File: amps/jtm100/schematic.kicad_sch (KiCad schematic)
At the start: 82 parts, among them T1 OT

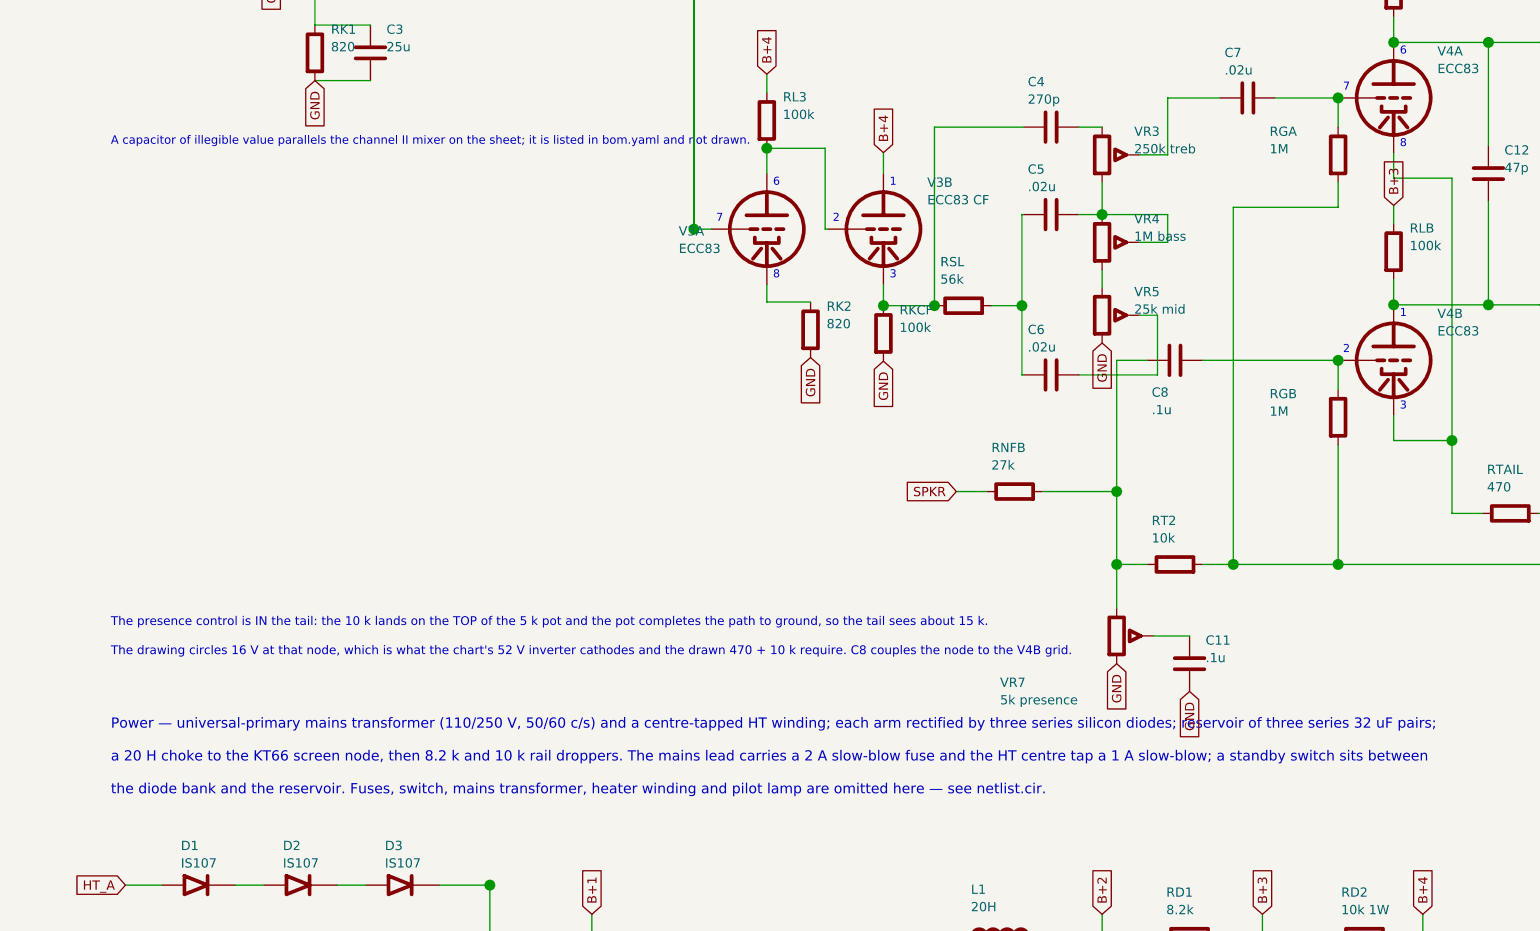
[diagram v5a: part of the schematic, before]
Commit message: Fix: schematic sheet notes no longer name repository files
Thirty-seven committed sheets rendered footnotes and section notes such as
"Heaters and PT primary omitted — see netlist.cir and meta.yaml" or
"excluded from netlist.cir (notes.md)" to visitors through KiCanvas. The
prose sweeps never counted sheets. Rewritten in the site's own words — the
netlist, the sources list, the circuit story, the parts list, the board
drawing — in 59 strings across 33 draw scripts, keeping every technical
claim as it was; the three tone sheets (6G4, 6G5, 6G6-B) are under repair
elsewhere and keep theirs for now. The sweep touched only strings passed to
the sheet's note, text, caption and footnote calls, never a path or a value.

Gates: check_schematics 40/0, connectivity 0 isolated pins;
verify_schematic_nets 40 clean; only the regenerated sheets and their served
copies changed.

Co-Authored-By: Claude Fable 5.1 <noreply@anthropic.com>
Claude-Session: https://claude.ai/code/session_01KBMfdh37HmCL2iWcBiL5J1
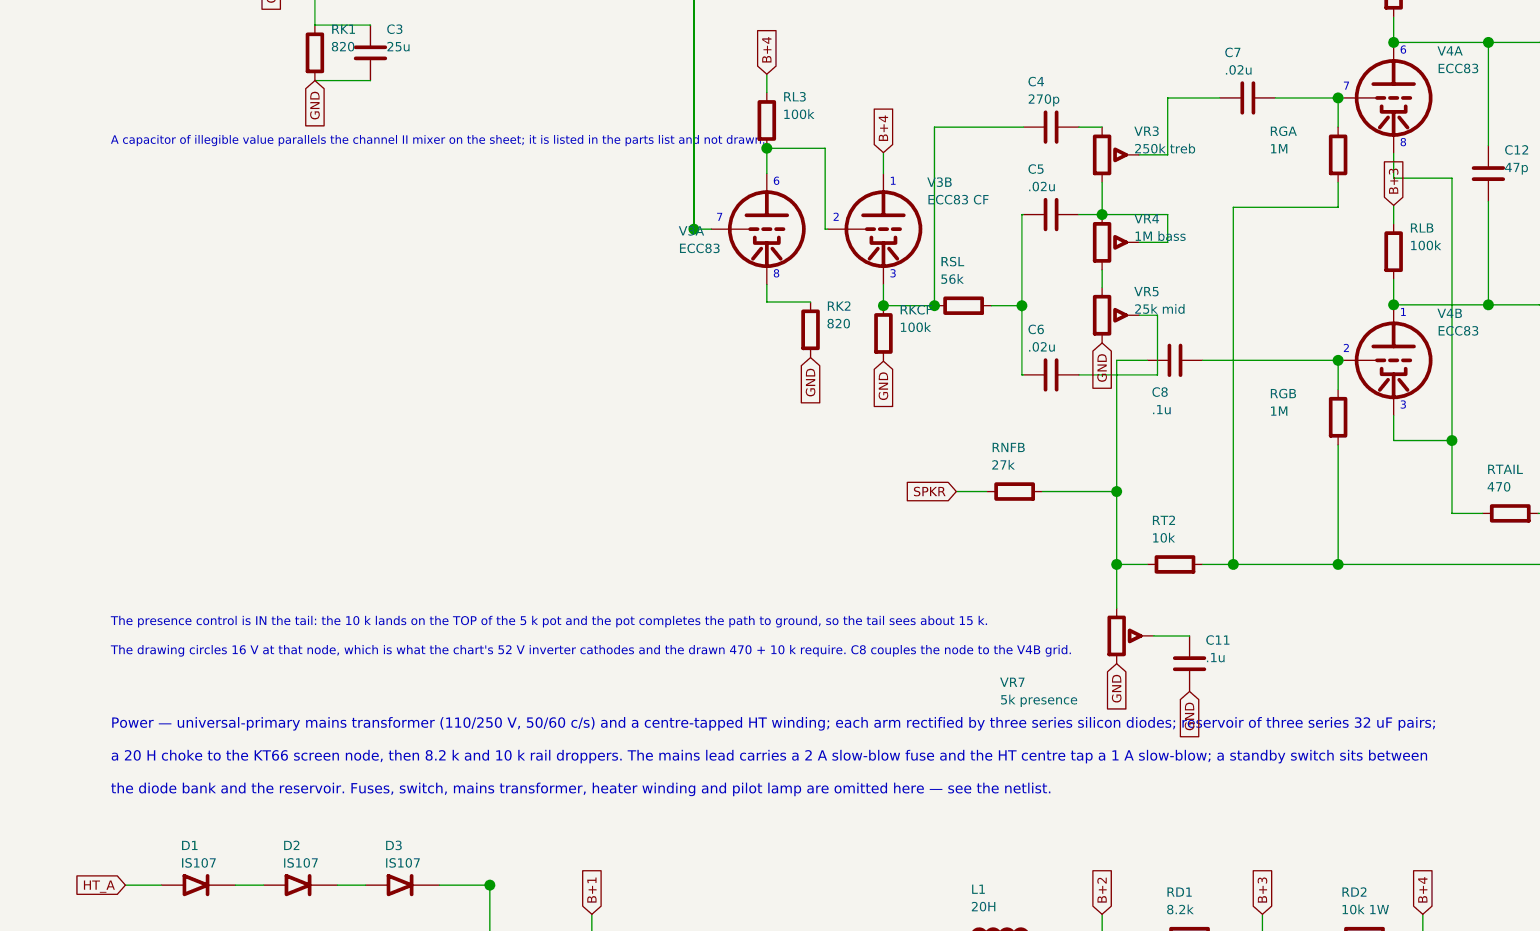
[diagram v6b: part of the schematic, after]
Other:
- note added: "A capacitor of illegible value parallels the channel II mixer on the sheet; it is listed in the parts list and not drawn."
- note added: "the diode bank and the reservoir. Fuses, switch, mains transformer, heater winding and pilot lamp are omitted here — see the netlist."
- note removed: "A capacitor of illegible value parallels the channel II mixer on the sheet; it is listed in bom.yaml and not drawn."
- note removed: "the diode bank and the reservoir. Fuses, switch, mains transformer, heater winding and pilot lamp are omitted here — see netlist.cir."
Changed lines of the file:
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@@
   (junction (at 101.336 66.988) (diameter 1.497) (color 0 0 0 0))
   (junction (at 101.336 118.278) (diameter 1.497) (color 0 0 0 0))
-  (text "A capacitor of illegible value parallels the channel II mixer on the sheet; it is listed in bom.yaml and not drawn." (at 21.336 106.278 0)
+  (text "A capacitor of illegible value parallels the channel II mixer on the sheet; it is listed in the parts list and not drawn." (at 21.336 106.278 0)
     (effects (font (size 1.15 1.15)) (justify left)))
   (wire (pts (xy 55.336 45.898) (xy 55.336 49.278))
@@
   (text "a 20 H choke to the KT66 screen node, then 8.2 k and 10 k rail droppers. The mains lead carries a 2 A slow-blow fuse and the HT centre tap a 1 A slow-blow; a standby switch sits between" (at 21.336 190.778 0)
     (effects (font (size 1.4 1.4)) (justify left)))
-  (text "the diode bank and the reservoir. Fuses, switch, mains transformer, heater winding and pilot lamp are omitted here — see netlist.cir." (at 21.336 195.278 0)
+  (text "the diode bank and the reservoir. Fuses, switch, mains transformer, heater winding and pilot lamp are omitted here — see the netlist." (at 21.336 195.278 0)
     (effects (font (size 1.4 1.4)) (justify left)))
   (global_label "HT_A" (shape input) (at 23.336 208.278 180)

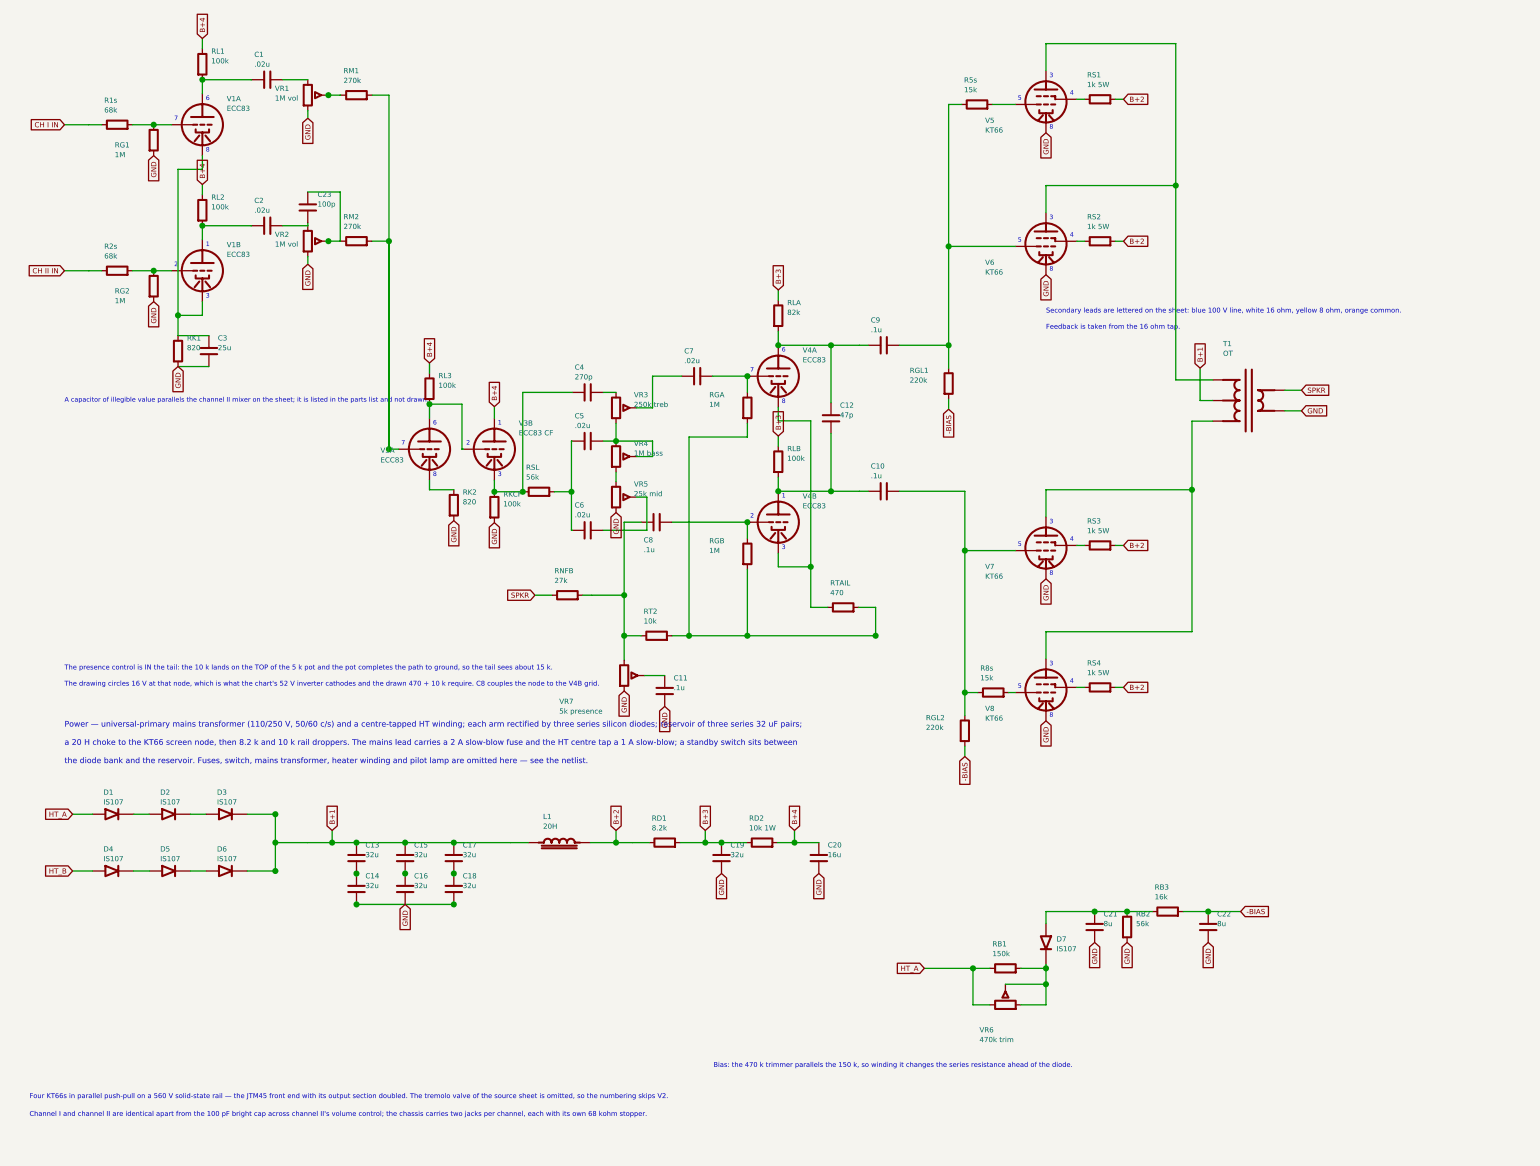
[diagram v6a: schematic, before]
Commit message: JTM100: each input jack has its own 68 kΩ stopper; leaks at jack 1's tip
The cited 1959T drawing (drtube 1959t-66.gif, 1068x759, sha1 94aa0ac9…)
draws four input jacks and four 68 Ks, two per channel (channel I pair crop
30,120,250,230 into V1A; channel II pair crop 30,230,250,340, its junction
running round to V1B's grid, crop 180,80,330,300), with each 1M from the
lower jack's tip line, jack side of its 68K, to ground. The BOM note said
the schematic draws one jack per channel, and the sheet hung the 1M on the
grid side of the stopper. R3s and R4s are added to the BOM and the sheet,
the leaks move to the jack-1 tip (R1s/R2s series_bridge in sch_map), and
the off-board scope glob widens to R[1-4]s. No DC node moves.

Co-Authored-By: Claude Opus 5.5 <noreply@anthropic.com>
Claude-Session: https://claude.ai/code/session_01KBMfdh37HmCL2iWcBiL5J1
Signed-off-by: AnalogMaker <theanalogmaker@gmail.com>
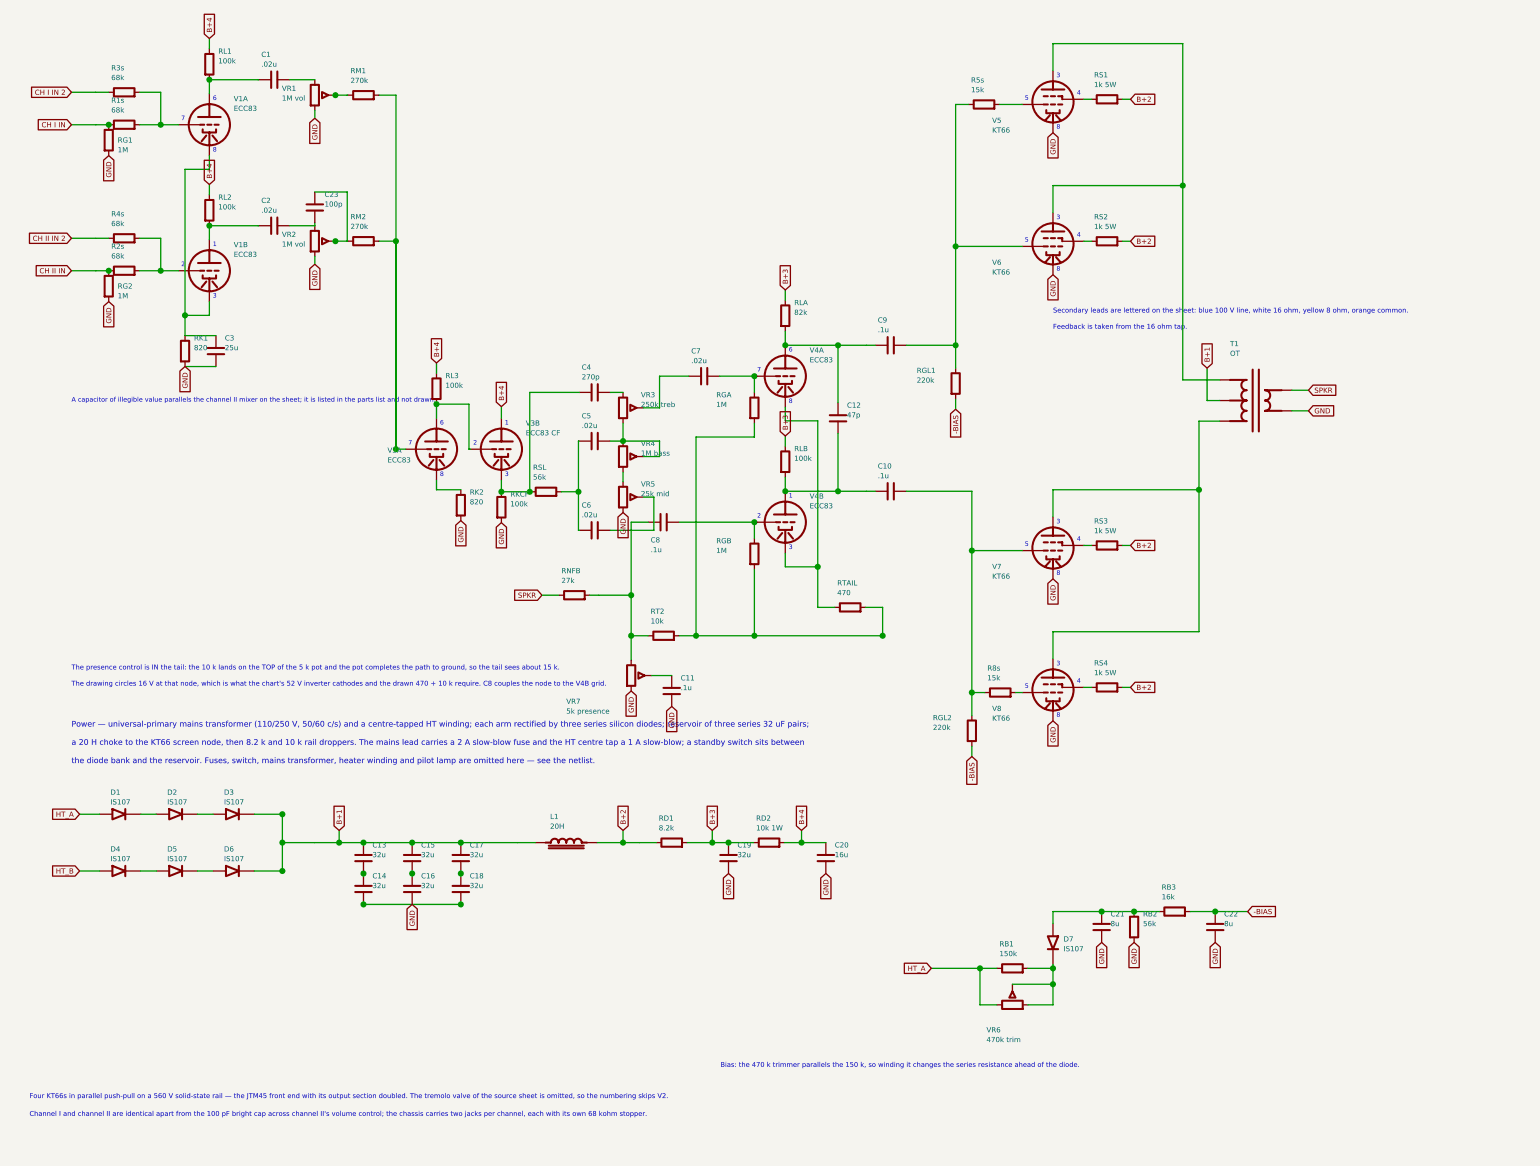
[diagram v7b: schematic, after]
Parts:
- removed C6: .02u, symbol cx:C
- removed C8: .1u, symbol cx:C
- removed D5: IS107, symbol cx:DIODE_SS
- removed L1: 20H, symbol cx:CHOKE
- removed RD2: 10k 1W, symbol cx:R
- removed RG2: 1M, symbol cx:R
- removed RGL1: 220k, symbol cx:R
- removed RKCF: 100k, symbol cx:R
- removed RM2: 270k, symbol cx:R
- removed V4A: ECC83, symbol cx:TRIODE
- removed V6, V8: KT66, symbol cx:PENTODE
- removed VR4: 1M bass, symbol cx:POT
- added C12: 47p, symbol cx:C
- added C15, C19: 32u, symbol cx:C
- added C2, C7: .02u, symbol cx:C
- added C23: 100p, symbol cx:C
- added R3s: 68k, symbol cx:R
- added R8s: 15k, symbol cx:R
- added RK1: 820, symbol cx:R
- added RS3: 1k 5W, symbol cx:R
- added T1: OT, symbol cx:OT_PP
- added V4B: ECC83, symbol cx:TRIODE
- added V5: KT66, symbol cx:PENTODE
- added VR3: 250k treb, symbol cx:POT
- added VR6: 470k trim, symbol cx:POT
- C10: renamed from R8s; value 15k -> .1u; symbol cx:R -> cx:C
- C6: renamed from V4B; value ECC83 -> .02u; symbol cx:TRIODE -> cx:C
- C8: renamed from RNFB; value 27k -> .1u; symbol cx:R -> cx:C
- D5: renamed from C15; value 32u -> IS107; symbol cx:C -> cx:DIODE_SS
- L1: renamed from C19; value 32u -> 20H; symbol cx:C -> cx:CHOKE
- R4s: renamed from C2; value .02u -> 68k; symbol cx:C -> cx:R
- RD2: renamed from VR6; value 470k trim -> 10k 1W; symbol cx:POT -> cx:R
- RG2: renamed from C23; value 100p -> 1M; symbol cx:C -> cx:R
- RGL1: renamed from RS3; value 1k 5W -> 220k
- RKCF: renamed from VR3; value 250k treb -> 100k; symbol cx:POT -> cx:R
- RM2: renamed from RK1; value 820 -> 270k
- RNFB: renamed from V5; value KT66 -> 27k; symbol cx:PENTODE -> cx:R
- V4A: renamed from C12; value 47p -> ECC83; symbol cx:C -> cx:TRIODE
- V6: renamed from C10; value .1u -> KT66; symbol cx:C -> cx:PENTODE
- V8: renamed from T1; value OT -> KT66; symbol cx:OT_PP -> cx:PENTODE
- VR4: renamed from C7; value .02u -> 1M bass; symbol cx:C -> cx:POT
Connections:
- net -BIAS: now also RGL1.2
- net B+1: now also L1.1, C15.1, T1.2 (CT); no longer D5.1, V8.2 (CT)
- net B+2: now also L1.2, RS3.2; no longer RGL1.2
- net B+3: now also RD2.1, C19.1; no longer L1.1
- net B+4: now also RD2.2
- net CH I IN: now also RG1.1
- net CH II IN: now also RG2.1
- net GND: now also RG2.2, RKCF.2, V6.4 (K), V8.4 (K), C19.2, RK1.2, T1.5 (SEC_C), V5.4 (K); no longer L1.2, RM2.2, RNFB.4 (K), V8.5 (SEC_C)
- net HT_A: now also VR6.1; no longer RD2.1
- net SPKR: now also RNFB.1, T1.4 (SEC_H); no longer C8.1, V8.4 (SEC_H)
- net at C3.1, V1A.3 (K), V1B.3 (K): now also RK1.1; no longer RM2.1
- net at D4.2 (K): now also D5.1 (A)
- net at D6.1 (A): now also D5.2 (K)
- net at C5.1, RSL.2: now also C6.1
- net at C5.2: now also VR4.1, VR4.2 (W), VR3.3; no longer RKCF.3
- net at RGL2.1, V7.2 (G1): now also C10.2, R8s.1; no longer C10.1, V6.2
- net at V8.1 (P): now also V7.1 (P), T1.3 (PRI_B); no longer RNFB.1 (P)
- net at V8.3 (G2): now also RS4.1; no longer V7.1 (P)
- net at C9.2, R5s.1: now also RGL1.1, V6.2 (G1)
- net at RS2.1: now also V6.3 (G2)
- net at RL2.2, V1B.1 (P): now also C2.1; no longer R4s.1
- net at C9.1, RLA.2, V4A.1 (P): now also C12.1
- net at C4.1, RSL.1, V3B.3 (K): now also RKCF.1
- net at C4.2: now also VR3.1; no longer RKCF.1
- net at RT2.1, VR7.1: now also C8.1, RNFB.2; no longer C8.2
- net at RTAIL.1: now also V4A.3 (K), V4B.3 (K); no longer C6.3 (K)
- net at V7.3 (G2): now also RS3.1; no longer RGL1.1
- net at R5s.2: now also V5.2 (G1); no longer RNFB.2 (G1)
- net at RGA.1: now also V4A.2 (G), C7.2; no longer VR4.2
- net at VR2.2 (W): now also RM2.1, C23.1; no longer RG2.1
- net at RM1.2, V3A.2 (G): now also RM2.2
- net at C6.2: now also VR5.2 (W); no longer RGB.1
- net at VR5.1: now also VR4.3
- net at C16.1: now also C15.2; no longer D5.2
- net at R1s.2, V1A.2 (G): now also R3s.2; no longer RG1.1
- net at RS1.1: now also V5.3 (G2); no longer RNFB.3 (G2)
- net at R2s.2, V1B.2 (G): now also R4s.2
- net at D7.2 (K), RB1.2: now also VR6.2 (W), VR6.3; no longer RD2.2 (W), RD2.3
- new net: R8s.2, V8.2 (G1)
- new net: C10.1, C12.2, RLB.2, V4B.1 (P)
- new net: C8.2, RGB.1, V4B.2 (G)
- new net: C7.1, VR3.2 (W)
- new net: T1.1 (PRI_A), V5.1 (P), V6.1 (P)
- new net: C2.2, C23.2, VR2.1
- new net CH I IN 2: R3s.1
- new net CH II IN 2: R4s.1
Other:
- moved on the sheet: D5, R1s, RGL1, RM2, V1A, V8
